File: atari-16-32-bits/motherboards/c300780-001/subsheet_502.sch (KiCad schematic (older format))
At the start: 26 parts, among them U500 74X374_OCTAL_D-TYPE_EDGE-TRIG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, U501 74X374_OCTAL_D-TYPE_EDGE-TRIG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, U502 DAC0802LCN_PHY, U503 DAC0802LCN_PHY

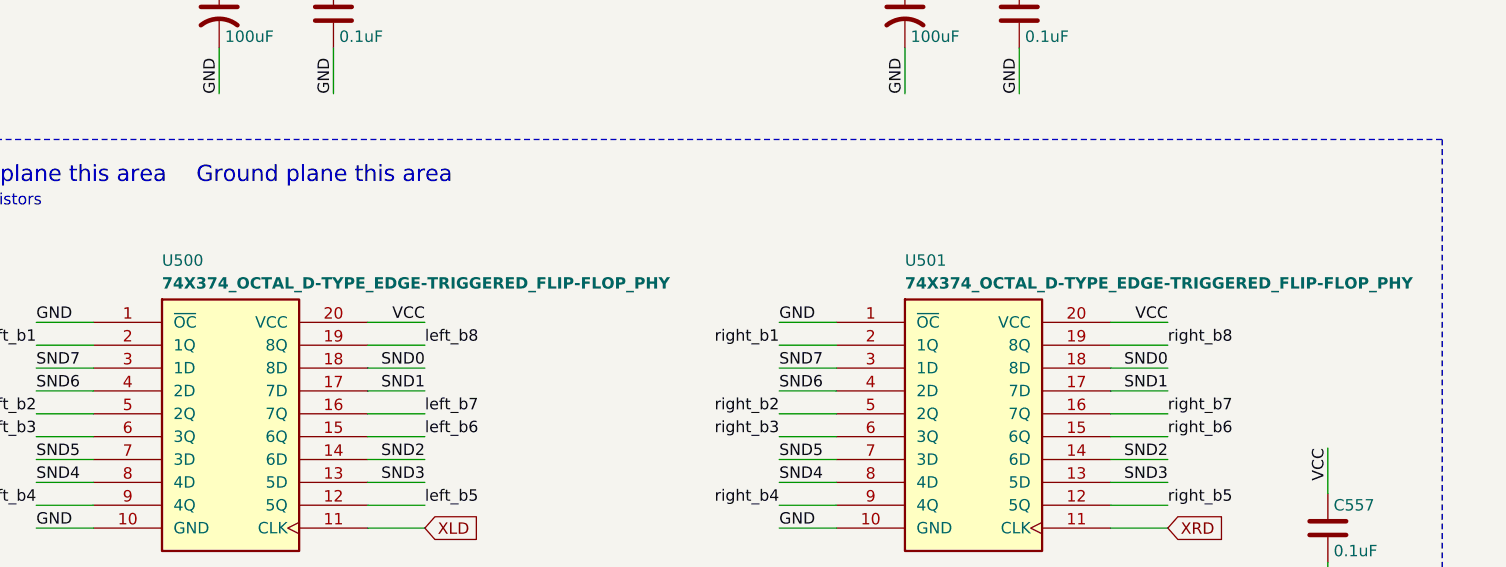
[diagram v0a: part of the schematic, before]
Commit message: Fixes #14 : [Atari STE] U500 and U501 are 74_F_374
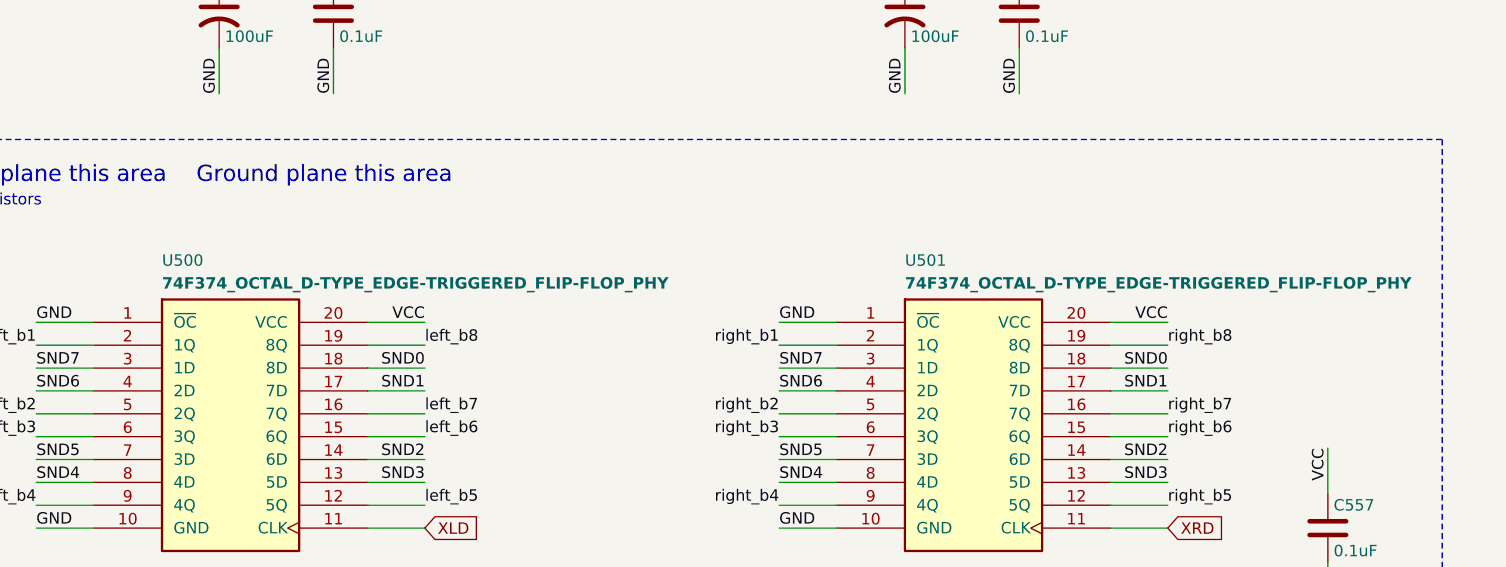
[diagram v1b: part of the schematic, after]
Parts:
- U500, U501: value 74X374_OCTAL_D-TYPE_EDGE-TRIGGERED_FLIP-FLOP_PHY -> 74F374_OCTAL_D-TYPE_EDGE-TRIGGERED_FLIP-FLOP_PHY
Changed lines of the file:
@@
 P 2450 3550
 F 0 "U500" H 2150 4300 50  0000 L TNN
-F 1 "74X374_OCTAL_D-TYPE_EDGE-TRIGGERED_FLIP-FLOP_PHY" H 2150 4200 50  0000 L TNB
+F 1 "74F374_OCTAL_D-TYPE_EDGE-TRIGGERED_FLIP-FLOP_PHY" H 2150 4200 50  0000 L TNB
 F 2 "Package_DIP:DIP-20_W7.62mm_LongPads" H 2150 4400 50  0001 L TNN
 F 3 "https://www.ti.com/lit/ds/symlink/sn54s373.pdf" H 2150 4500 50  0001 L TNN
@@
 P 5700 3550
 F 0 "U501" H 5400 4300 50  0000 L TNN
-F 1 "74X374_OCTAL_D-TYPE_EDGE-TRIGGERED_FLIP-FLOP_PHY" H 5400 4200 50  0000 L TNB
+F 1 "74F374_OCTAL_D-TYPE_EDGE-TRIGGERED_FLIP-FLOP_PHY" H 5400 4200 50  0000 L TNB
 F 2 "Package_DIP:DIP-20_W7.62mm_LongPads" H 5400 4400 50  0001 L TNN
 F 3 "https://www.ti.com/lit/ds/symlink/sn54s373.pdf" H 5400 4500 50  0001 L TNN

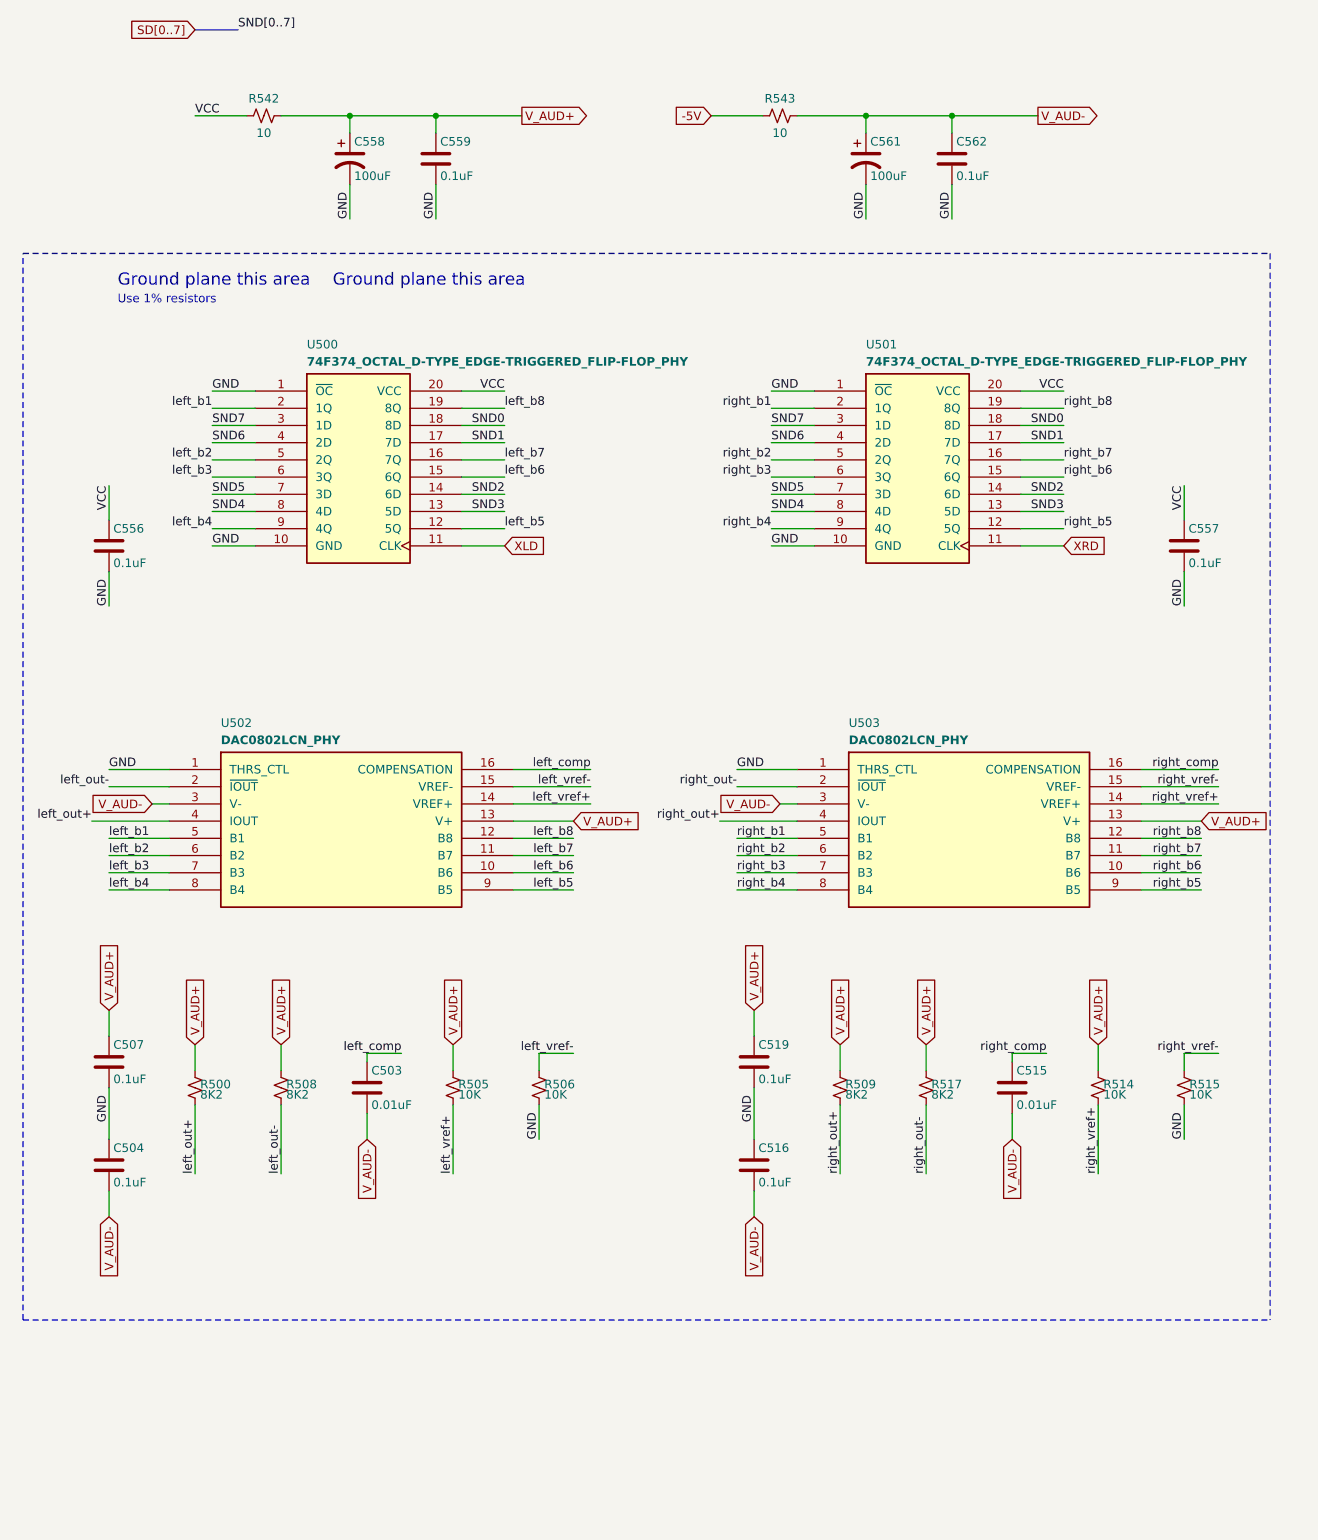
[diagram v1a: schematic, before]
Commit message: Resolves #15 : [Atari STE] Rework the audio circuit for better understandability
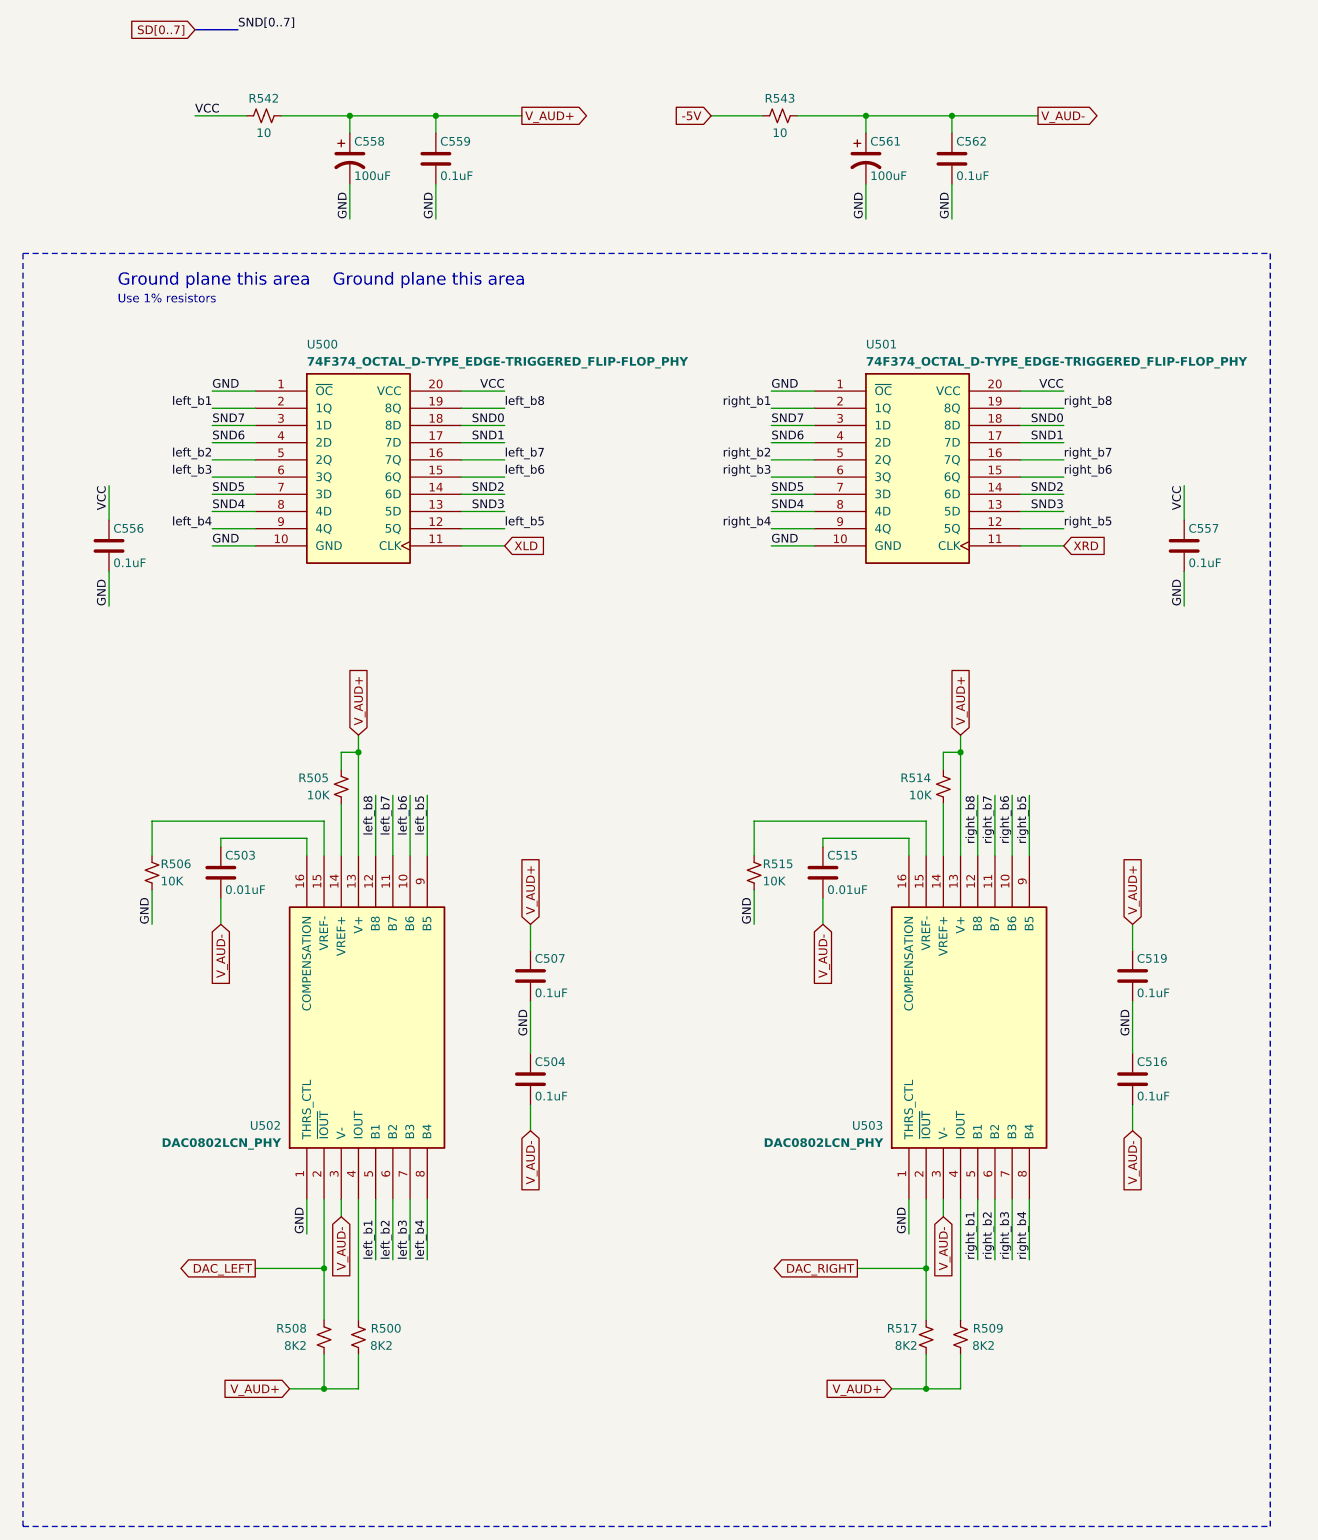
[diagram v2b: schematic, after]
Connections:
- net left_comp: no longer names the net of C503.1, U502.16 (COMPENSATION)
- net left_out+: no longer names the net of R500.2, U502.4 (IOUT)
- net left_out- renamed DAC_LEFT
- net left_vref+: no longer names the net of R505.2, U502.14 (VREF+)
- net left_vref-: no longer names the net of R506.1, U502.15 (VREF-)
- net right_comp: no longer names the net of C515.1, U503.16 (COMPENSATION)
- net right_out+: no longer names the net of R509.2, U503.4 (IOUT)
- net right_out- renamed DAC_RIGHT
- net right_vref+: no longer names the net of R514.2, U503.14 (VREF+)
- net right_vref-: no longer names the net of R515.1, U503.15 (VREF-)
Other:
- moved on the sheet: C503, C504, C507, C515, C516, C519, R500, R505, R506, R508, R509, R514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

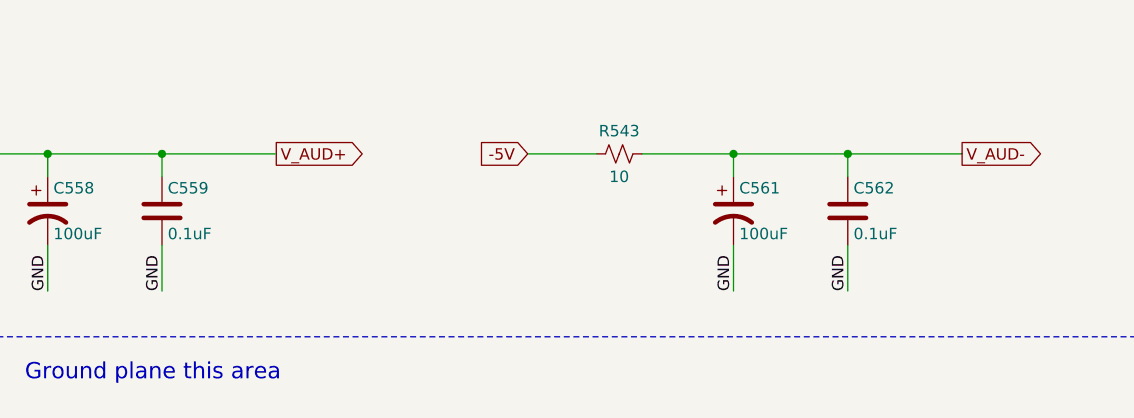
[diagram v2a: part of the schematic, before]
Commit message: Resolves #39 : [ERC] Create power symbols for regulated voltages
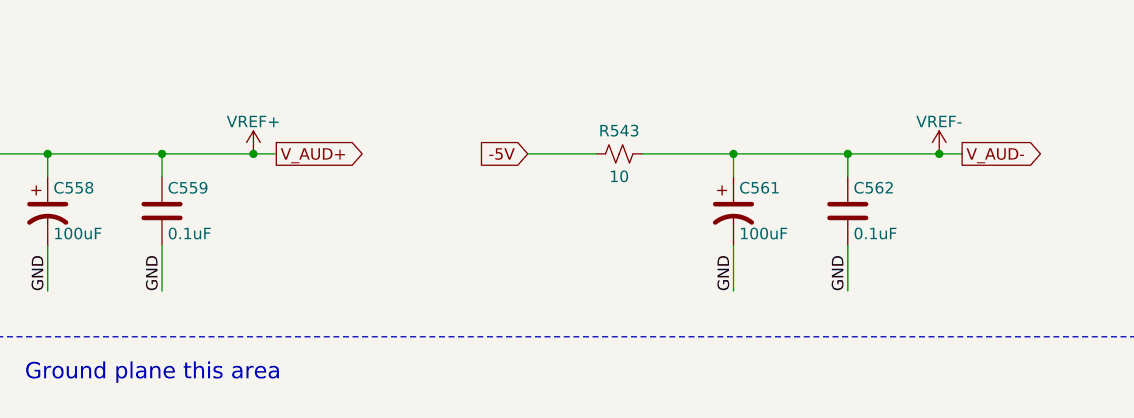
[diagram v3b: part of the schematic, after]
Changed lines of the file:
@@
 Text Label 7250 3650 3    50   ~ 0
 VCC
-Text GLabel 3400 1500 2    50   Output ~ 0
-V_AUD+
 Wire Wire Line
 	2000 1500 2400 1500
@@
 Connection ~ 2900 1500
 Wire Wire Line
-	2900 1500 3400 1500
-Text GLabel 6400 1500 2    50   Output ~ 0
-V_AUD-
-Wire Wire Line
 	5000 1500 5400 1500
 Wire Wire Line
@@
 Connection ~ 5900 1500
 Wire Wire Line
-	5900 1500 6400 1500
+	5900 1500 6300 1500
 Text Notes 1050 2500 0    71   ~ 0
 Ground plane this area
@@
 Wire Wire Line
 	5350 8200 5750 8200
+$Comp
+L vref:VREF+ #PWR0104
+U 1 1 60E05E7B
+P 3300 1500
+F 0 "#PWR0104" H 3300 1350 50  0001 C CNN
+F 1 "VREF+" H 3300 1640 50  0000 C CNN
+F 2 "" H 3300 1500 50  0001 C CNN
+F 3 "" H 3300 1500 50  0001 C CNN
+	1    3300 1500
+	1    0    0    -1
+$EndComp
+$Comp
+L vref:VREF- #PWR0105
+U 1 1 60E067FA
+P 6300 1500
+F 0 "#PWR0105" H 6300 1350 50  0001 C CNN
+F 1 "VREF-" H 6300 1640 50  0000 C CNN
+F 2 "" H 6300 1500 50  0001 C CNN
+F 3 "" H 6300 1500 50  0001 C CNN
+	1    6300 1500
+	1    0    0    -1
+$EndComp
+Text GLabel 6400 1500 2    50   Output ~ 0
+V_AUD-
+Text GLabel 3400 1500 2    50   Output ~ 0
+V_AUD+
+Connection ~ 3300 1500
+Wire Wire Line
+	3300 1500 3400 1500
+Wire Wire Line
+	2900 1500 3300 1500
+Connection ~ 6300 1500
+Wire Wire Line
+	6300 1500 6400 1500
 $EndSCHEMATC
